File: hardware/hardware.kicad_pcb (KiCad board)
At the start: 4 copper layers, 44.2 x 37 mm, 55 parts, among them J1 JST-PH, J2 SWD Debug, J3 COMPANION, J4 CAM PWR, Q1 AO3401A, SW1 SW_Push, U1 TPS562202S, U2 TPS562202S, U3 STM32G071KBUxN, U4 INA226

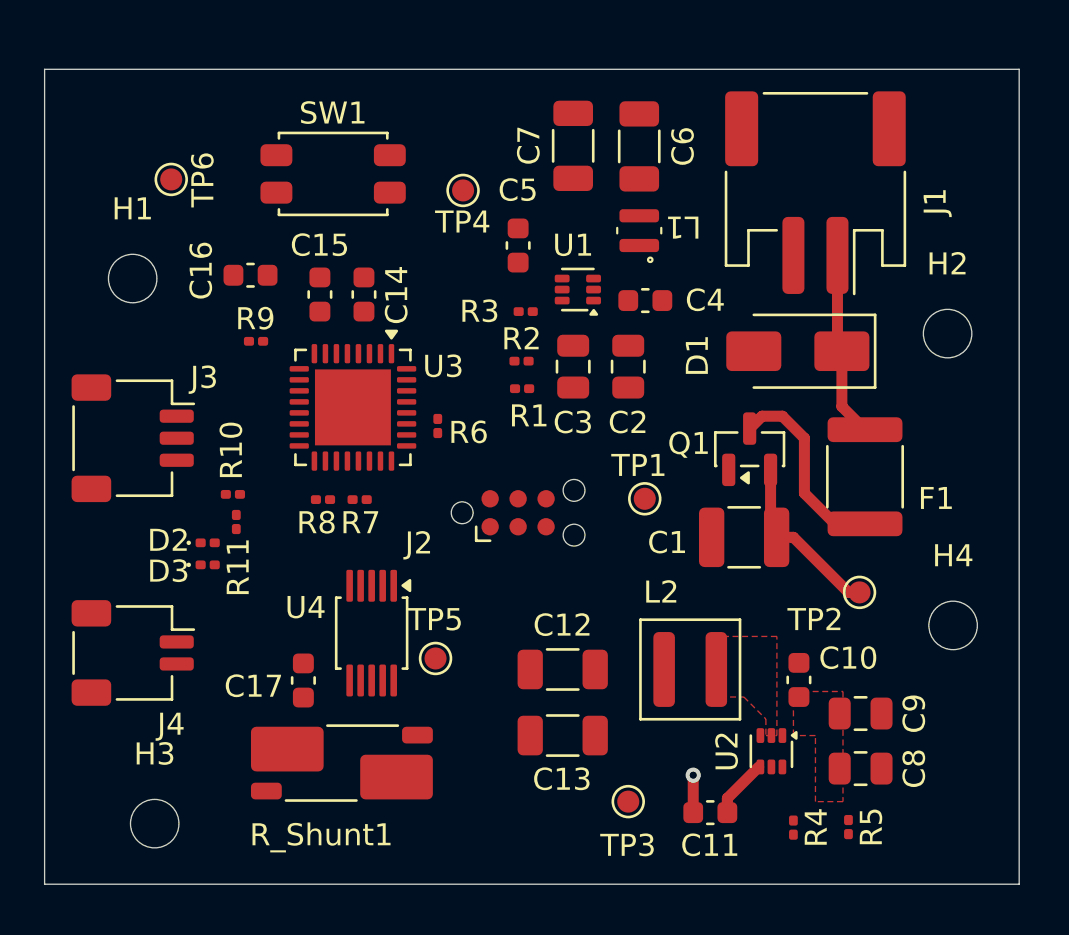
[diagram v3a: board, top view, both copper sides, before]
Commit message: Completed PCB and passed DRC
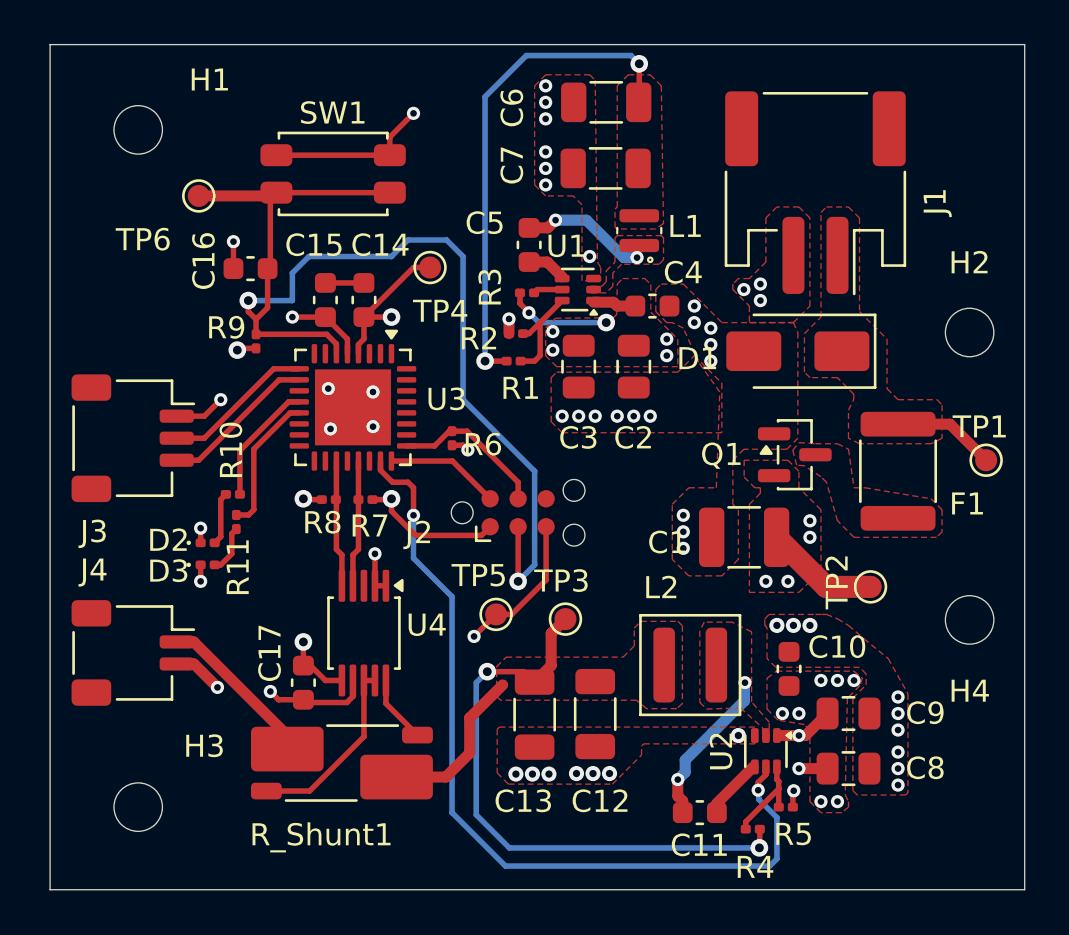
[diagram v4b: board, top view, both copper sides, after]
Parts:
- moved TP1 15.6 mm to (158.8, 73.0)
- moved TP3 8.76 mm to (139.6, 80.2)
- moved H1 6.75 mm to (120.2, 58.0)
- moved TP4 3.81 mm to (133.5, 64.2)
- moved TP5 3.40 mm to (136.5, 80.0)
- moved R5 2.99 mm to (149.7, 88.8), turned to 180 degrees
- moved C12 2.51 mm to (141.0, 84.5), turned to -90 degrees
- moved C6 2.50 mm to (141.5, 56.8), turned to 180 degrees
- moved Q1 2.07 mm to (150.1, 72.8), turned to 0 degrees
- moved R4 1.85 mm to (148.2, 89.8), turned to 0 degrees
- moved C7 1.80 mm to (141.5, 59.8), turned to 180 degrees
- moved C13 1.59 mm to (138.2, 84.5), turned to -90 degrees
- moved F1 1.52 mm to (154.8, 73.5)
- moved TP6 1.46 mm to (123.0, 61.0)
- moved R1 1.31 mm to (137.3, 68.5)
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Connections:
- U3 pad 15: /MCU/EN_RAILB -> unconnected-(U3-PB0-Pad15)
- U3 pad 23: unconnected-(U3-PA10/PA12-Pad23) -> /MCU/EN_RAILB
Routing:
- net /Connectors_Comms/RESET: track 0.00 -> 51.6 mm, vias 0 -> 2
- net /Connectors_Comms/3V3: track 0.00 -> 41.0 mm, vias 0 -> 7
- net GND: track 0.00 -> 39.4 mm, vias 0 -> 57
- net /MCU/EN_RAILB: track 0.00 -> 38.3 mm, vias 0 -> 2
- net /Current_Sense/5V: track 0.00 -> 33.6 mm, vias 0 -> 2
- net Net-(Q1-D): track 8.96 -> 0.00 mm
- net /Current_Sense/VIN-: track 0.00 -> 8.50 mm
- net /Current_Sense/VBAT_PROT: track 7.97 -> 15.9 mm, vias 0 -> 19
- net /Connectors_Comms/5V_CAM: track 0.00 -> 7.40 mm
- net /Connectors_Comms/USART2_RX: track 0.00 -> 7.07 mm
- net /Connectors_Comms/SWCLK_BOOT0: track 0.00 -> 7.05 mm
- net /Connectors_Comms/USART2_TX: track 0.00 -> 6.87 mm
- net Net-(U3-PA6): track 0.00 -> 6.39 mm
- net /Current_Sense/I2C1_SDA: track 0.00 -> 5.77 mm
- net /Current_Sense/I2C1_SCL: track 0.00 -> 5.77 mm
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- added copper zone on F.Cu, net /Connectors_Comms/3V3
- added copper zone on In2.Cu, net /Connectors_Comms/3V3
- added copper zone on F.Cu, net /Current_Sense/5V
- added copper zone on In2.Cu, net /Current_Sense/VBAT_PROT
- added copper zone on F.Cu, net /Current_Sense/VBAT_RAW
- added copper zone on F.Cu, net GND
- added copper zone on F.Cu, net Net-(Q1-D)
- added copper zone on F.Cu, net Net-(U1-SW)
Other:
- board size 44.2 x 37 mm -> 44.2 x 38.4 mm

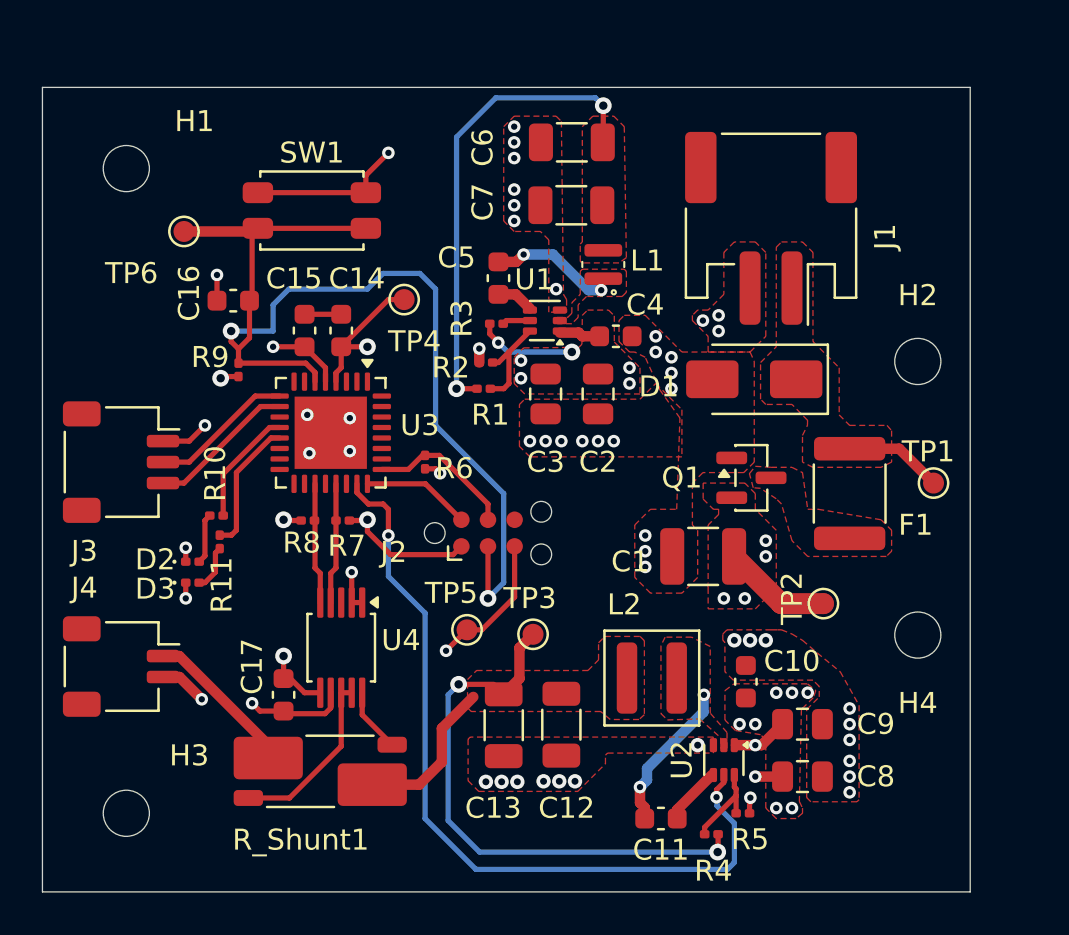
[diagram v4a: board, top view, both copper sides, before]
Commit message: PCB V1.1
Board completed, updated with labels for external connectors. Corrected and tightened hot loop with better layout and routing
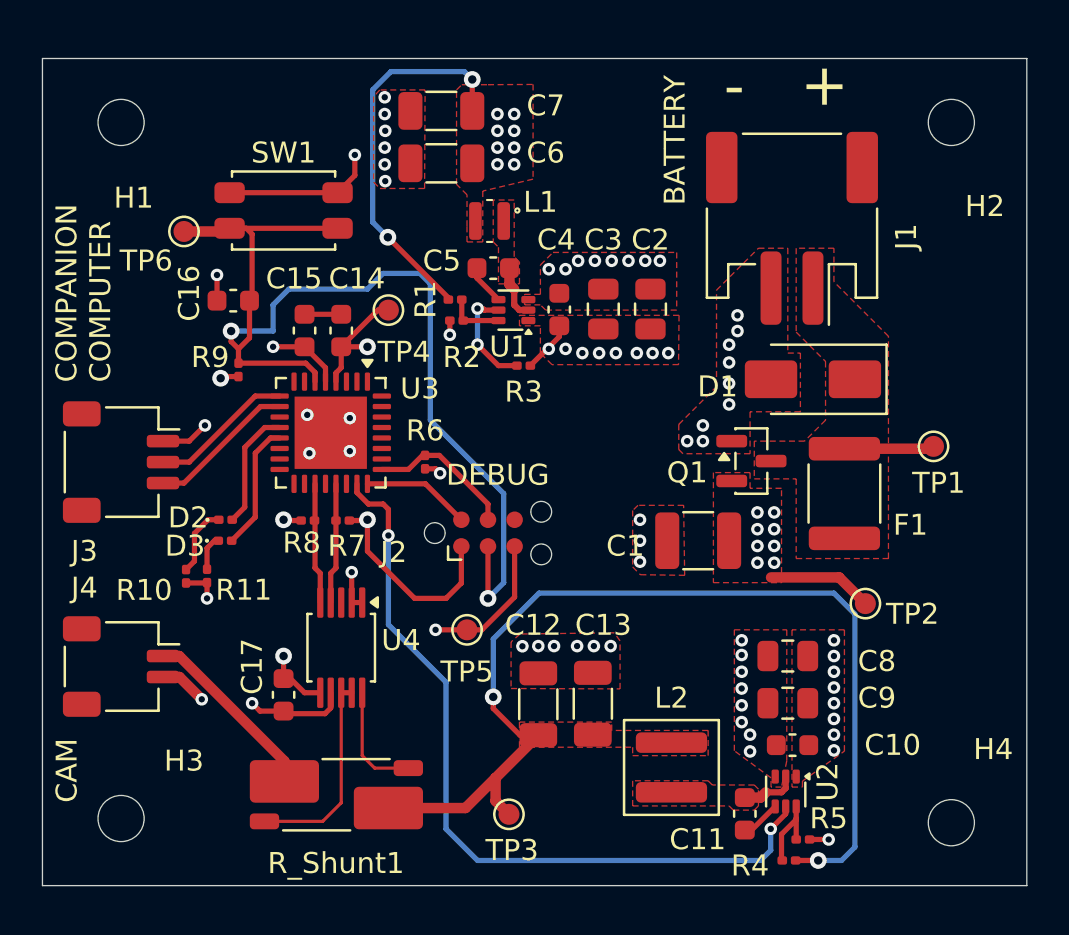
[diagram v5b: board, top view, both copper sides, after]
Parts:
- moved H2 11.5 mm to (159.6, 55.8)
- moved H4 9.09 mm to (159.6, 89.2)
- moved TP3 8.66 mm to (138.5, 88.8), turned to 90 degrees
- moved C7 7.66 mm to (135.3, 55.2)
- moved C6 6.30 mm to (135.3, 57.8)
- moved L1 5.81 mm to (137.6, 60.5), turned to 180 degrees
- moved C8 5.79 mm to (151.8, 81.2), turned to 180 degrees
- moved C3 4.90 mm to (143.0, 64.7), turned to 90 degrees
- moved C2 4.76 mm to (145.2, 64.7), turned to 90 degrees
- moved R1 4.46 mm to (135.9, 64.2)
- moved C13 4.37 mm to (142.5, 83.5), turned to 90 degrees
- moved L2 4.37 mm to (146.2, 86.6), turned to 90 degrees
- moved C11 4.01 mm to (149.8, 88.8), turned to 90 degrees
- moved R4 3.91 mm to (151.9, 91.0)
- moved C10 3.76 mm to (152.0, 85.5), turned to 180 degrees
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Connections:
- D2 pad 1: GND -> Net-(D2-K)
- D3 pad 1: GND -> Net-(D3-K)
- F1 pad 2: Net-(Q1-D) -> /Current_Sense/VBAT_RAW
- Q1 pad 3: Net-(Q1-D) -> /Current_Sense/VBAT_RAW
- R10 pad 1: Net-(U3-PA5) -> Net-(D2-K)
- R10 pad 2: Net-(D2-A) -> GND
- R11 pad 1: Net-(U3-PA6) -> Net-(D3-K)
- R11 pad 2: Net-(D3-A) -> GND
- U3 pad 12: Net-(U3-PA5) -> Net-(D2-A)
- U3 pad 13: Net-(U3-PA6) -> Net-(D3-A)
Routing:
- net /Current_Sense/5V: track 33.6 -> 49.4 mm
- net /Current_Sense/VBAT_PROT: track 15.9 -> 7.49 mm, vias 19 -> 24
- net Net-(U3-PA6): track 6.39 -> 0.00 mm
- net Net-(U3-PA5): track 5.60 -> 0.00 mm
- net Net-(U2-SW): track 7.26 -> 2.69 mm, vias 2 -> 0
- net Net-(D3-A): track 2.19 -> 6.10 mm
- net Net-(U1-EN): track 1.34 -> 5.05 mm, vias 0 -> 2
- net Net-(D2-A): track 2.41 -> 5.75 mm
- net Net-(D2-K): track 0.00 -> 3.32 mm
- net Net-(U1-SW): track 5.75 -> 2.62 mm, vias 2 -> 0
- net /Current_Sense/VIN+: track 3.07 -> 5.45 mm
- net Net-(U1-VFB): track 4.88 -> 2.71 mm
- net /Connectors_Comms/3V3: track 41.0 -> 38.9 mm, vias 7 -> 15
- net Net-(D3-K): track 0.00 -> 1.69 mm
- net /Connectors_Comms/5V_CAM: track 7.40 -> 8.83 mm
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- removed copper zone on F.Cu, net Net-(Q1-D)
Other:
- board size 44.2 x 38.4 mm -> 46.9 x 39.5 mm
- board text added: "+"
- board text added: "-"
- board text added: "BATTERY"
- board text added: "CAM"
- board text added: "COMPANION COMPUTER"
- board text added: "DEBUG"
